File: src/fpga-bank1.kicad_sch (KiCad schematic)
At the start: 21 parts

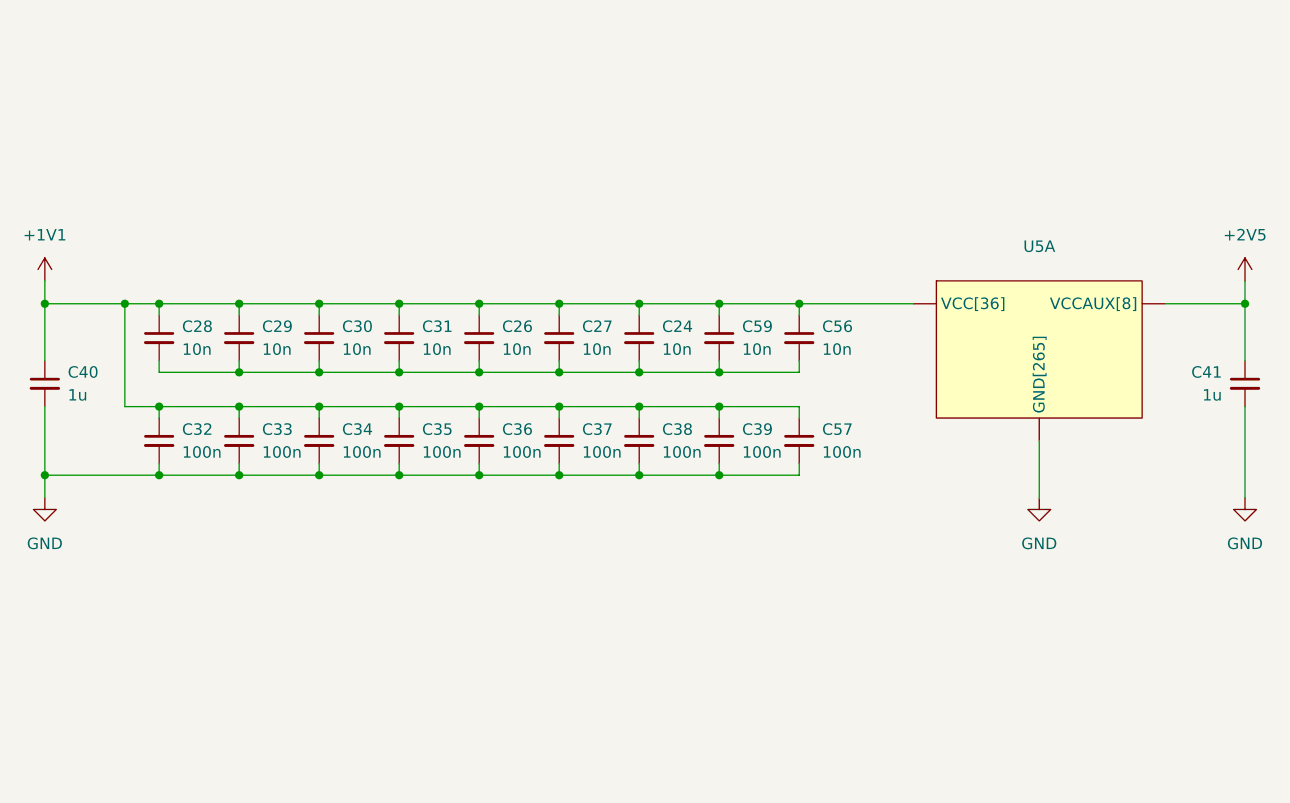
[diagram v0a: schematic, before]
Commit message: Adds more FPGA IO banks
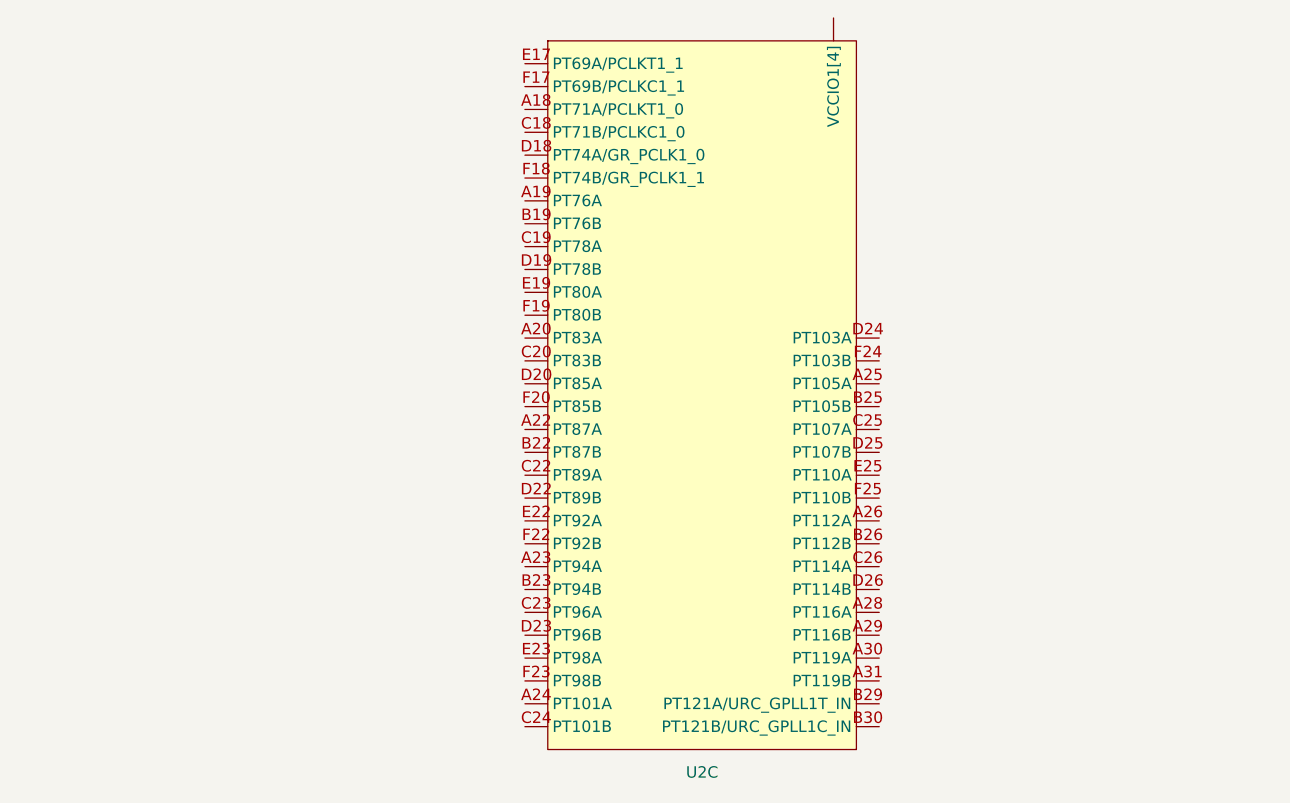
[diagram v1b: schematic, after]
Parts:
- removed C24, C26, C27, C28, C29, C30, C31, C56, C59: 10n, symbol Device:C_Small
- removed C32, C33, C34, C35, C36, C37, C38, C39, C57: 100n, symbol Device:C_Small
- removed C40, C41: 1u, symbol Device:C_Small
- removed U5: ~, symbol ECAP5-BSOM:LFE5U-85F-*BG756*
- added U2: ~, symbol ECAP5-BSOM:LFE5U-85F-*BG756*
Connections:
- new net VCCIO1: U2. (VCCIO1[4]), U2.K17 (VCCIO1), U2.K18 (VCCIO1), U2.K19 (VCCIO1), U2.K21 (VCCIO1)
